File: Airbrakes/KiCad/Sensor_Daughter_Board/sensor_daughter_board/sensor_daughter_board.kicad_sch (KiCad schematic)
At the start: 11 parts, among them U1 BMI088, U2 BMP581, U3 BMM350

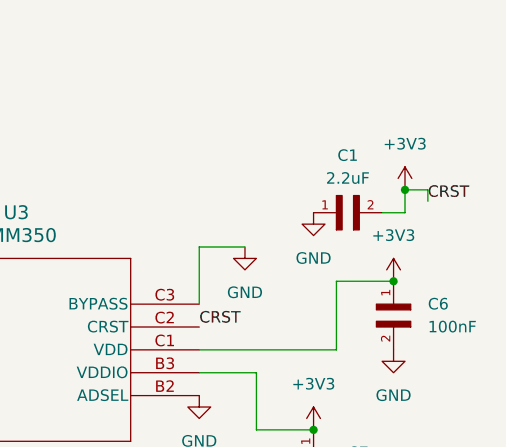
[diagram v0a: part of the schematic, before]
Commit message: make edge connected .2 mm smaller
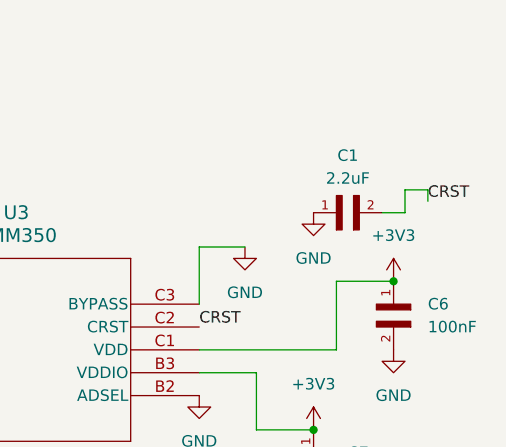
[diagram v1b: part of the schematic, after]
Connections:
- net +3V3: no longer C1.2, U3.C2 (CRST)
- new net CRST: C1.2, U3.C2 (CRST)
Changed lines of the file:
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@@
-	)
-	(junction
-		(at 271.78 48.26)
-		(diameter 0)
-		(color 0 0 0 0)
 	)
 	(junction
@@
 					(unit 1)
 				)
-			)
-		)
-	)
-	(symbol
-		(lib_id "power:+3V3")
-		(at 271.78 48.26 0)
-		(unit 1)
-		(exclude_from_sim no)
-		(in_bom yes)
-		(on_board yes)
-		(dnp no)
-		(fields_autoplaced yes)
-		(property "Reference" "#PWR015"
-			(at 271.78 52.07 0)
-			(effects
-				(font
-					(size 1.27 1.27)
-				)
-				(hide yes)
-			)
-		)
-		(property "Value" "+3V3"
-			(at 271.78 43.18 0)
-			(effects
-				(font
-					(size 1.27 1.27)
-				)
-			)
-		)
-		(property "Footprint" ""
-			(at 271.78 48.26 0)
-			(effects
-				(font
-					(size 1.27 1.27)
-				)
-				(hide yes)
-			)
-		)
-		(property "Datasheet" ""
-			(at 271.78 48.26 0)
-			(effects
-				(font
-					(size 1.27 1.27)
-				)
-				(hide yes)
-			)
-		)
-		(property "Description" "Power symbol creates a global label with name \"+3V3\""
-			(at 271.78 48.26 0)
-			(effects
-				(font
-					(size 1.27 1.27)
-				)
-				(hide yes)
-			)
-		)
-		(pin "1"
-		)
-		(instances
-			(project "sensor_daughter_board"
-				(path "/d11b09a8-fa1c-477d-8cab-cf1dcdbb31ee"
-					(reference "#PWR015")
-					(unit 1)
-				)
